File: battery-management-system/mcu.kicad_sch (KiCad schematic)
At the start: 2 parts

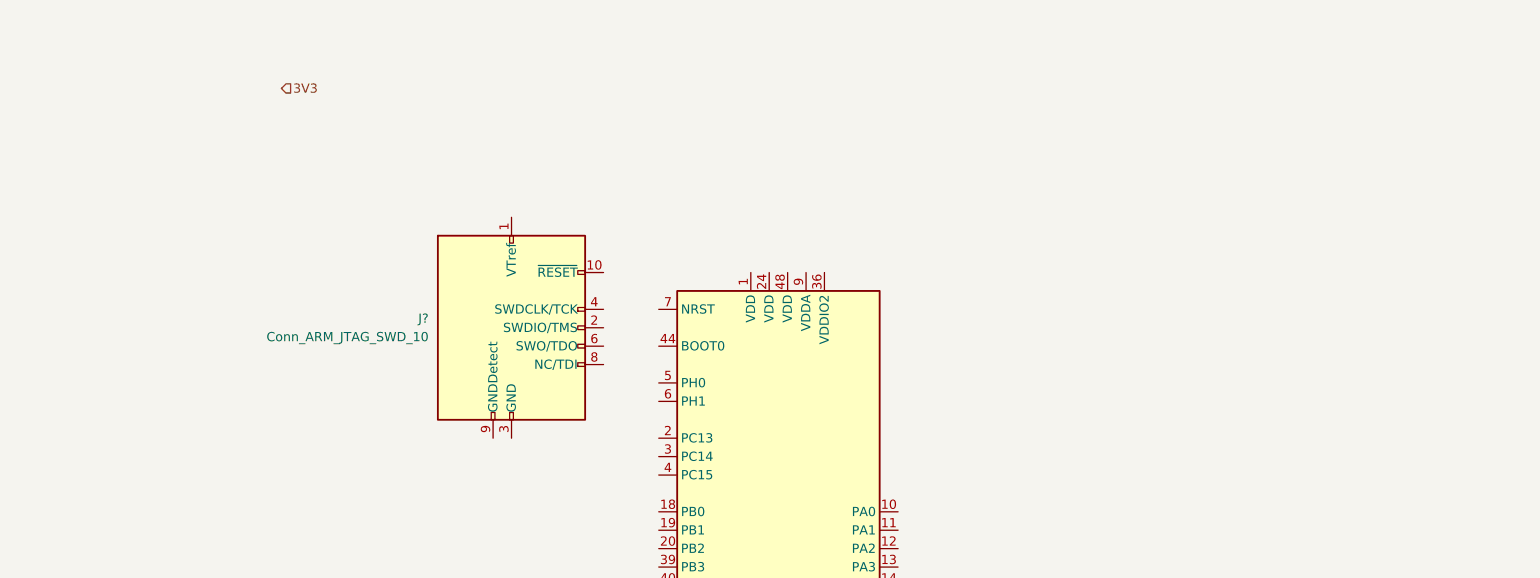
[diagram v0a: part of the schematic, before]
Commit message: define basic hierarchy and power supplies
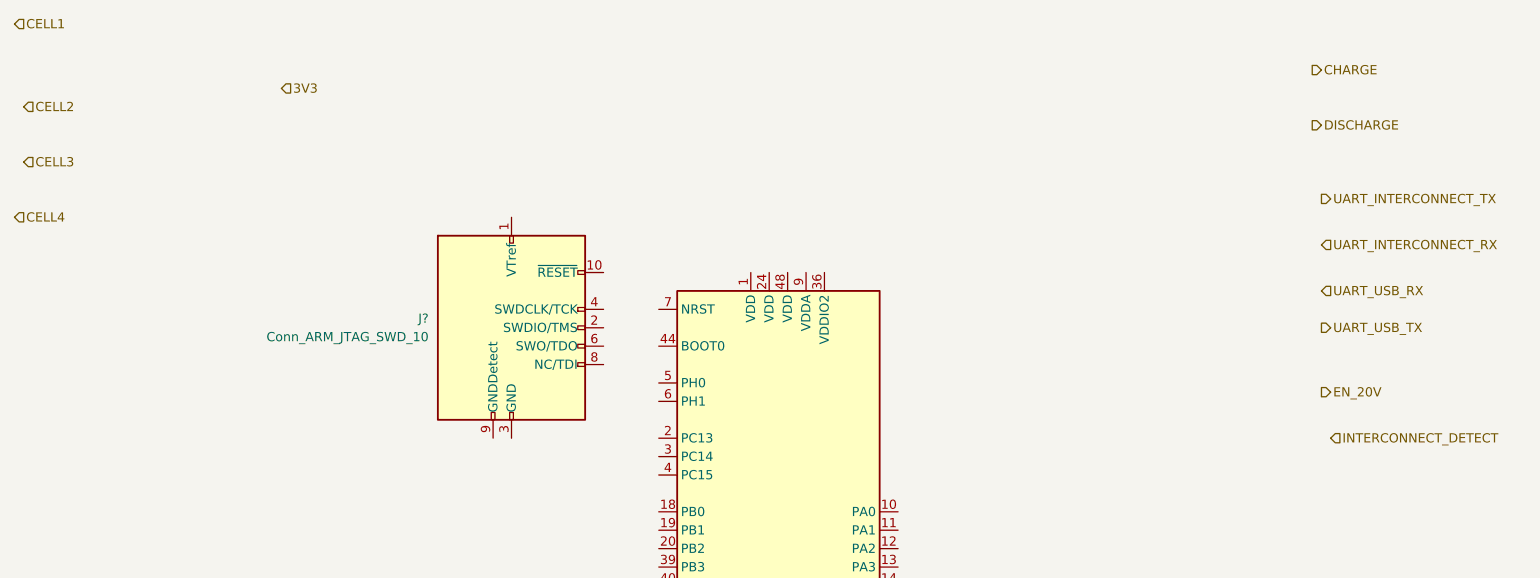
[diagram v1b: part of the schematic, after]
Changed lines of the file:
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@@
 (kicad_sch (version 20211123) (generator eeschema)
   (paper "A4")
+  (hierarchical_label "INTERCONNECT_DETECT" (shape input) (at 209.55 88.9 0)
+    (effects (font (size 1.27 1.27)) (justify left))
+  )
+  (hierarchical_label "UART_USB_TX" (shape output) (at 208.28 73.66 0)
+    (effects (font (size 1.27 1.27)) (justify left))
+  )
+  (hierarchical_label "EN_20V" (shape output) (at 208.28 82.55 0)
+    (effects (font (size 1.27 1.27)) (justify left))
+  )
   (hierarchical_label "3V3" (shape input) (at 64.77 40.64 0)
     (effects (font (size 1.27 1.27)) (justify left))
   )
+  (hierarchical_label "UART_USB_RX" (shape input) (at 208.28 68.58 0)
+    (effects (font (size 1.27 1.27)) (justify left))
+  )
+  (hierarchical_label "CELL1" (shape input) (at 27.94 31.75 0)
+    (effects (font (size 1.27 1.27)) (justify left))
+  )
+  (hierarchical_label "UART_INTERCONNECT_RX" (shape input) (at 208.28 62.23 0)
+    (effects (font (size 1.27 1.27)) (justify left))
+  )
+  (hierarchical_label "CELL4" (shape input) (at 27.94 58.42 0)
+    (effects (font (size 1.27 1.27)) (justify left))
+  )
+  (hierarchical_label "CHARGE" (shape output) (at 207.01 38.1 0)
+    (effects (font (size 1.27 1.27)) (justify left))
+  )
+  (hierarchical_label "UART_INTERCONNECT_TX" (shape output) (at 208.28 55.88 0)
+    (effects (font (size 1.27 1.27)) (justify left))
+  )
+  (hierarchical_label "CELL3" (shape input) (at 29.21 50.8 0)
+    (effects (font (size 1.27 1.27)) (justify left))
+  )
+  (hierarchical_label "DISCHARGE" (shape output) (at 207.01 45.72 0)
+    (effects (font (size 1.27 1.27)) (justify left))
+  )
+  (hierarchical_label "CELL2" (shape input) (at 29.21 43.18 0)
+    (effects (font (size 1.27 1.27)) (justify left))
+  )

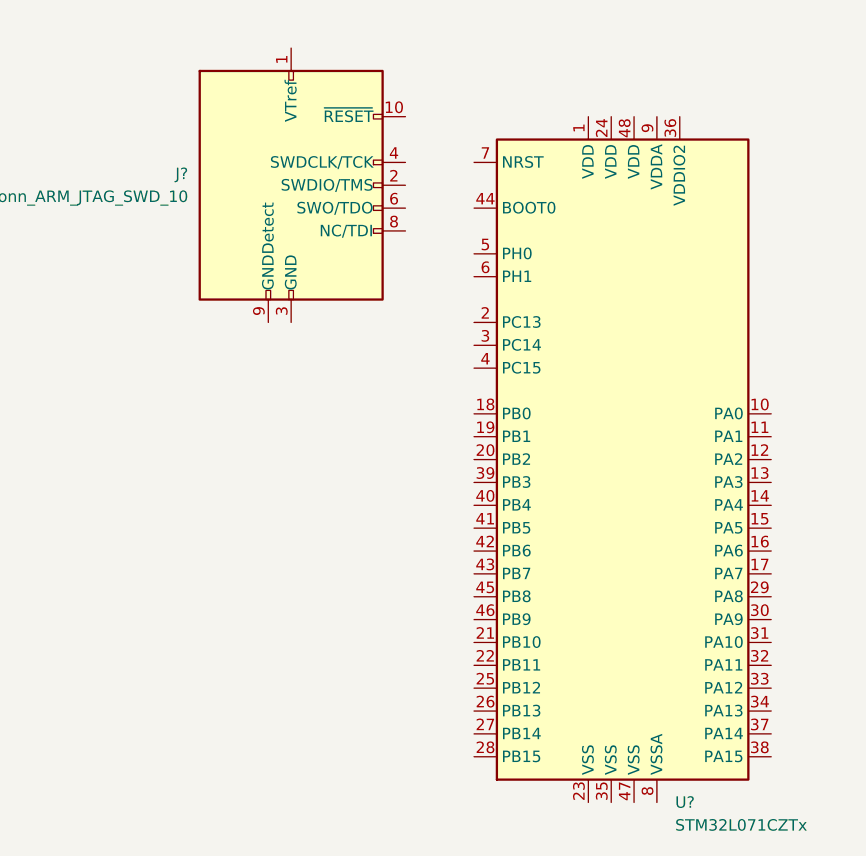
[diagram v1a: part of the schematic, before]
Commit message: add RS order numbers
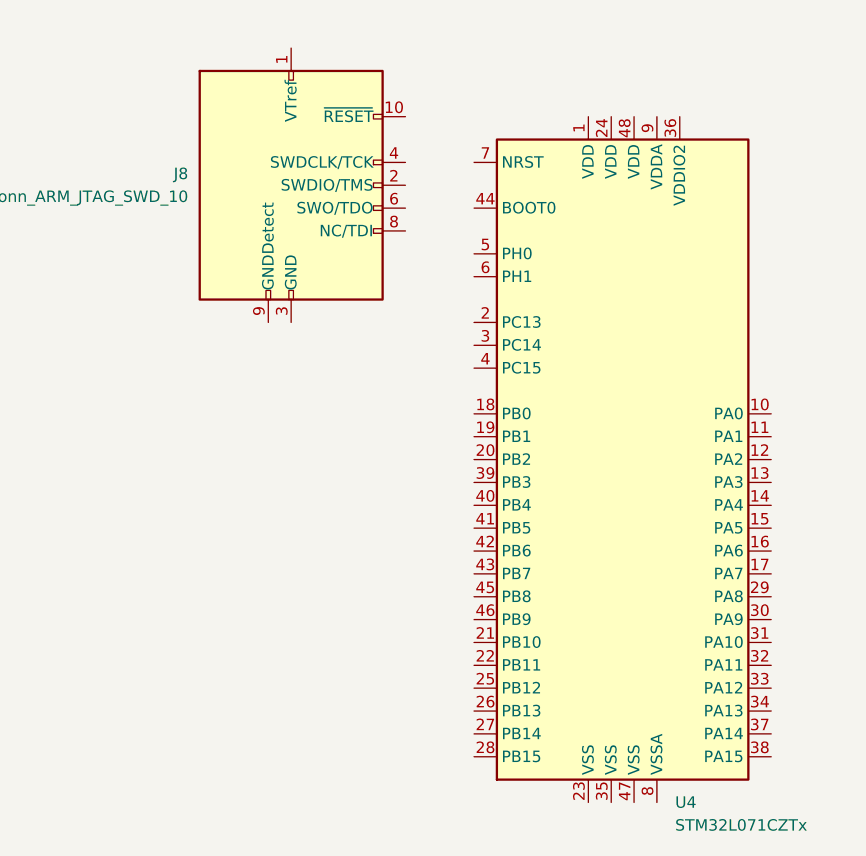
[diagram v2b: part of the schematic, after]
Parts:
- J8: renamed from J?; symbol Connector:Conn_ARM_JTAG_SWD_10 -> benediktibk:Conn_ARM_JTAG_SWD_10
- gave numbers to parts that had none: 1
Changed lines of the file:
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@@
   (symbol (lib_id "MCU_ST_STM32L0:STM32L071CZTx") (at 134.62 104.14 0) (unit 1)
     (in_bom yes) (on_board yes) (fields_autoplaced)
-    (property "Reference" "U?" (id 0) (at 139.1794 142.24 0)
+    (property "Reference" "U4" (id 0) (at 139.1794 142.24 0)
       (effects (font (size 1.27 1.27)) (justify left))
     )
@@
     (pin "9")
   )
-  (symbol (lib_id "Connector:Conn_ARM_JTAG_SWD_10") (at 96.52 73.66 0) (unit 1)
+  (symbol (lib_id "benediktibk:Conn_ARM_JTAG_SWD_10") (at 96.52 73.66 0) (unit 1)
     (in_bom yes) (on_board yes) (fields_autoplaced)
-    (property "Reference" "J?" (id 0) (at 85.09 72.3899 0)
+    (property "Reference" "J8" (id 0) (at 85.09 72.3899 0)
       (effects (font (size 1.27 1.27)) (justify right))
     )

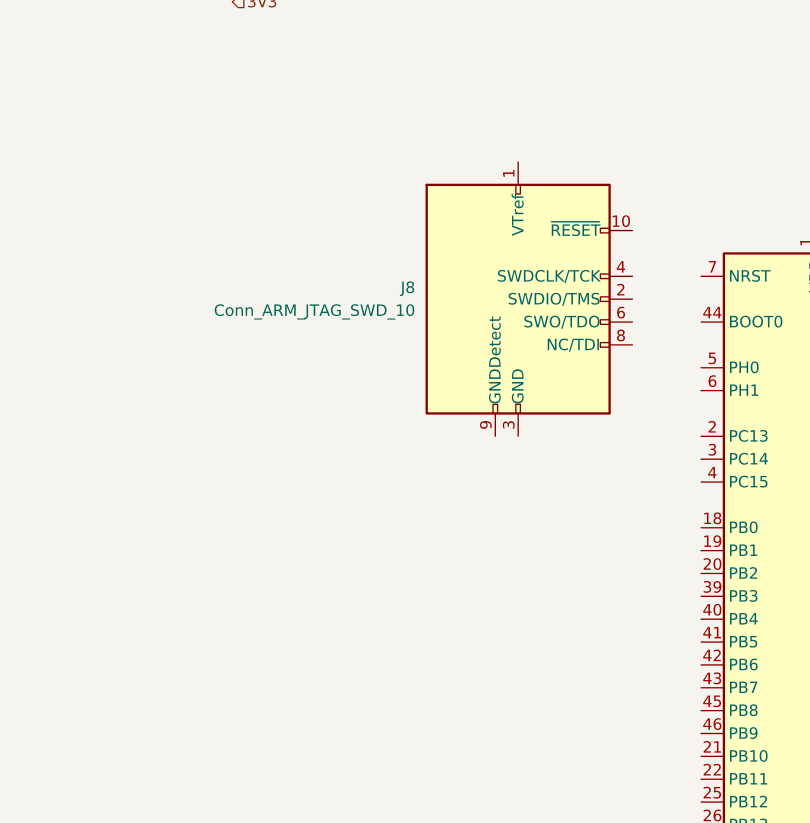
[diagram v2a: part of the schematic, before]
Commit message: add missing order numbers
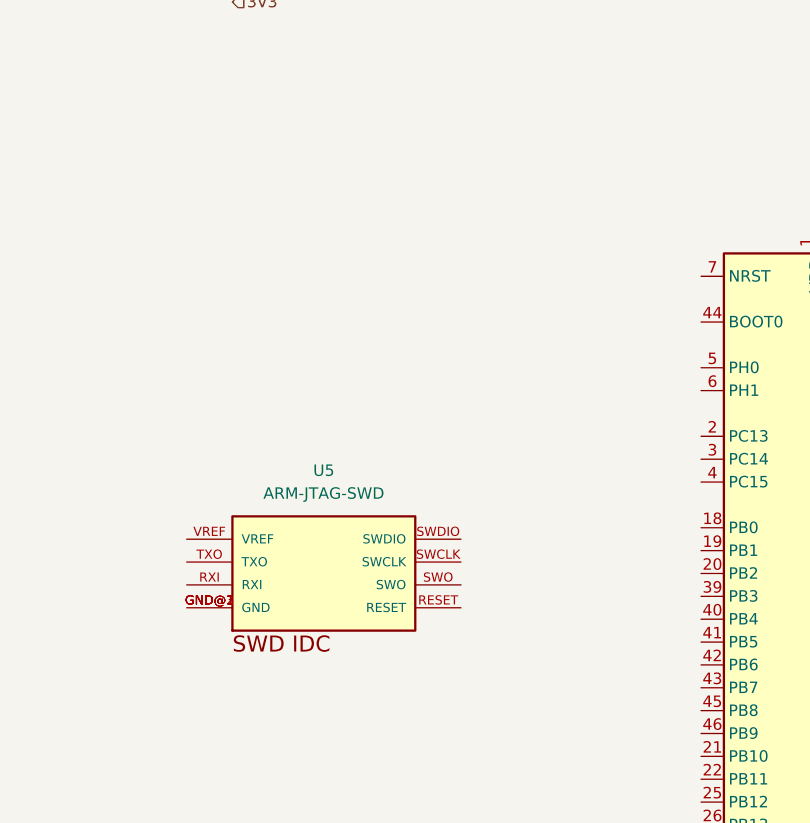
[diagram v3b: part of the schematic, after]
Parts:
- removed J8: Conn_ARM_JTAG_SWD_10, symbol benediktibk:Conn_ARM_JTAG_SWD_10
- added U5: ARM-JTAG-SWD, ARM-JTAG-SWD:ARM-JTAG-10-SWD-IDC, symbol benediktibk:ARM-JTAG-SWD
- U4: symbol MCU_ST_STM32L0:STM32L071CZTx -> benediktibk:STM32L071CZTx; RS order number (none) -> 196-2075
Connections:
- new net: U5.GND@1 (GND), U5.GND@2 (GND), U5.GND@3 (GND)
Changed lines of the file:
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@@
     (effects (font (size 1.27 1.27)) (justify left))
   )
-  (symbol (lib_id "MCU_ST_STM32L0:STM32L071CZTx") (at 134.62 104.14 0) (unit 1)
+  (symbol (lib_id "benediktibk:STM32L071CZTx") (at 134.62 104.14 0) (unit 1)
     (in_bom yes) (on_board yes) (fields_autoplaced)
     (property "Reference" "U4" (id 0) (at 139.1794 142.24 0)
@@
     )
     (property "Datasheet" "http://www.st.com/st-web-ui/static/active/en/resource/technical/document/datasheet/DM00141136.pdf" (id 3) (at 134.62 104.14 0)
+      (effects (font (size 1.27 1.27)) hide)
+    )
+    (property "RS order number" "196-2075" (id 4) (at 134.62 104.14 0)
       (effects (font (size 1.27 1.27)) hide)
     )
@@
     (pin "9")
   )
-  (symbol (lib_id "benediktibk:Conn_ARM_JTAG_SWD_10") (at 96.52 73.66 0) (unit 1)
+  (symbol (lib_id "benediktibk:ARM-JTAG-SWD") (at 67.31 105.41 0) (unit 1)
     (in_bom yes) (on_board yes) (fields_autoplaced)
-    (property "Reference" "J8" (id 0) (at 85.09 72.3899 0)
-      (effects (font (size 1.27 1.27)) (justify right))
+    (property "Reference" "U5" (id 0) (at 74.93 92.71 0))
+    (property "Value" "ARM-JTAG-SWD" (id 1) (at 74.93 95.25 0))
+    (property "Footprint" "ARM-JTAG-SWD:ARM-JTAG-10-SWD-IDC" (id 2) (at 67.31 105.41 0)
+      (effects (font (size 1.27 1.27)) (justify bottom) hide)
     )
-    (property "Value" "Conn_ARM_JTAG_SWD_10" (id 1) (at 85.09 74.9299 0)
-      (effects (font (size 1.27 1.27)) (justify right))
-    )
-    (property "Footprint" "" (id 2) (at 96.52 73.66 0)
+    (property "Datasheet" "" (id 3) (at 67.31 105.41 0)
       (effects (font (size 1.27 1.27)) hide)
     )
-    (property "Datasheet" "http://infocenter.arm.com/help/topic/com.arm.doc.ddi0314h/DDI0314H_coresight_components_trm.pdf" (id 3) (at 87.63 105.41 90)
+    (property "Description" "Cortex M JTAG/SWD 10 pin connector" (id 4) (at 67.31 105.41 0)
+      (effects (font (size 1.27 1.27)) (justify bottom) hide)
+    )
+    (property "RS order number" "159-2372" (id 5) (at 67.31 105.41 0)
       (effects (font (size 1.27 1.27)) hide)
     )
-    (pin "1")
-    (pin "10")
-    (pin "2")
-    (pin "3")
-    (pin "4")
-    (pin "5")
-    (pin "6")
-    (pin "7")
-    (pin "8")
-    (pin "9")
+    (pin "GND@1")
+    (pin "GND@2")
+    (pin "GND@3")
+    (pin "RESET")
+    (pin "RXI")
+    (pin "SWCLK")
+    (pin "SWDIO")
+    (pin "SWO")
+    (pin "TXO")
+    (pin "VREF")
   )
 )

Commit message: use own symbols and footprints
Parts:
- U4: footprint Package_QFP:LQFP-48_7x7mm_P0.5mm -> benediktibk:LQFP-48_7x7mm_P0.5mm
- U5: footprint ARM-JTAG-SWD:ARM-JTAG-10-SWD-IDC -> benediktibk:ARM-JTAG-10-SWD-IDC
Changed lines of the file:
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@@
       (effects (font (size 1.27 1.27)) (justify left))
     )
-    (property "Footprint" "Package_QFP:LQFP-48_7x7mm_P0.5mm" (id 2) (at 119.38 139.7 0)
+    (property "Footprint" "benediktibk:LQFP-48_7x7mm_P0.5mm" (id 2) (at 119.38 139.7 0)
       (effects (font (size 1.27 1.27)) (justify right) hide)
     )
@@
     (property "Reference" "U5" (id 0) (at 74.93 92.71 0))
     (property "Value" "ARM-JTAG-SWD" (id 1) (at 74.93 95.25 0))
-    (property "Footprint" "ARM-JTAG-SWD:ARM-JTAG-10-SWD-IDC" (id 2) (at 67.31 105.41 0)
+    (property "Footprint" "benediktibk:ARM-JTAG-10-SWD-IDC" (id 2) (at 67.31 105.41 0)
       (effects (font (size 1.27 1.27)) (justify bottom) hide)
     )
